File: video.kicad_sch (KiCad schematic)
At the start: 75 parts, among them IC11 MC14053, IC14 74LS86AN, IC21 74LS74, IC22 74LS00N, IC23 74ALS74N, IC27 74LS20N, IC28 74LS393N, IC29 74LS393N, IC30 74LS32N, IC32 74LS390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

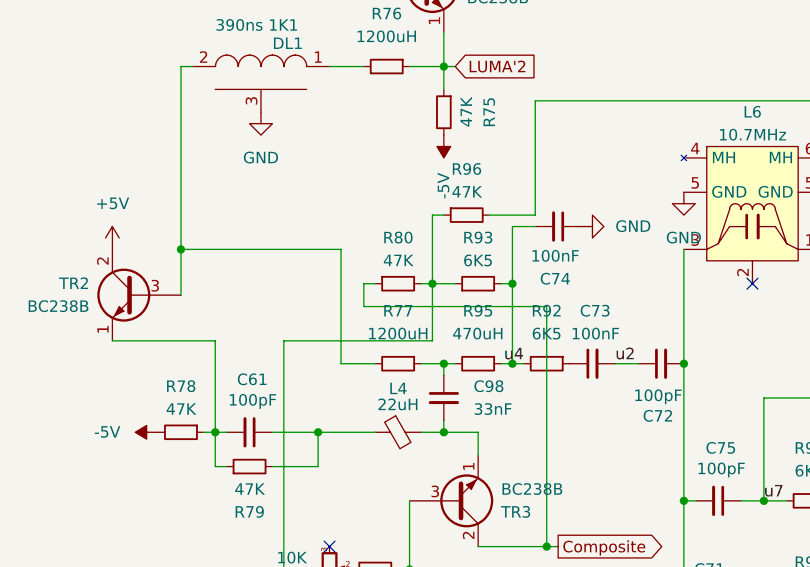
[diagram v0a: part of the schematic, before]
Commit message: add missing power connections
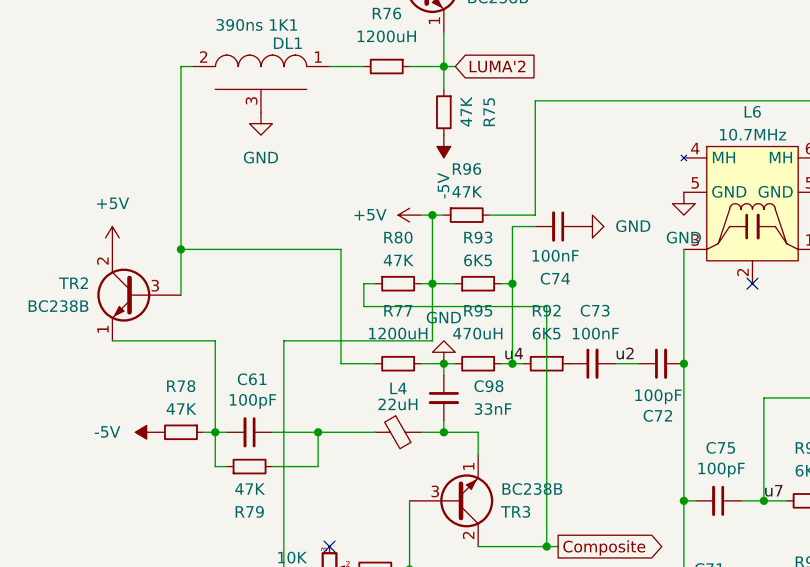
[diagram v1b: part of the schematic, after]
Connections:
- net +5V: now also R80.2, R82.1, R93.1, R96.1
- net GND: now also C98.1, R77.1, R95.2
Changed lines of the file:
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@@
 	)
 	(junction
+		(at 349.25 60.96)
+		(diameter 0)
+		(color 0 0 0 0)
+	)
+	(junction
 		(at 346.71 100.33)
 		(diameter 0)
@@
 	(wire
 		(pts
+			(xy 347.98 60.96) (xy 349.25 60.96)
+		)
+		(stroke
+			(width 0)
+			(type default)
+		)
+	)
+	(wire
+		(pts
 			(xy 143.51 89.535) (xy 145.669 89.535)
 		)
@@
 	)
 	(symbol
-		(lib_name "vdg:TOKO_Variable_Inductor")
 		(lib_id "vdg:TOKO_Variable_Inductor")
 		(at 384.81 58.42 0)
@@
 	)
 	(symbol
+		(lib_id "power:GND")
+		(at 350.52 77.47 0)
+		(mirror x)
+		(unit 1)
+		(exclude_from_sim no)
+		(in_bom yes)
+		(on_board yes)
+		(dnp no)
+		(fields_autoplaced yes)
+		(property "Reference" "#PWR0196"
+			(at 350.52 71.12 0)
+			(effects
+				(font
+					(size 1.27 1.27)
+				)
+				(hide yes)
+			)
+		)
+		(property "Value" "GND"
+			(at 350.52 72.39 0)
+			(effects
+				(font
+					(size 1.27 1.27)
+				)
+			)
+		)
+		(property "Footprint" ""
+			(at 350.52 77.47 0)
+			(effects
+				(font
+					(size 1.27 1.27)
+				)
+				(hide yes)
+			)
+		)
+		(property "Datasheet" ""
+			(at 350.52 77.47 0)
+			(effects
+				(font
+					(size 1.27 1.27)
+				)
+				(hide yes)
+			)
+		)
+		(property "Description" ""
+			(at 350.52 77.47 0)
+			(effects
+				(font
+					(size 1.27 1.27)
+				)
+				(hide yes)
+			)
+		)
+		(pin "1"
+		)
+		(instances
+			(project "Dragon32Issue2ASecam"
+				(path "/e3d9e4a2-26cb-4482-98c1-138d9a22d1eb/abc062f3-c6ab-4360-94b7-a88968b74324"
+					(reference "#PWR0196")
+					(unit 1)
+				)
+			)
+		)
+	)
+	(symbol
 		(lib_id "Device:R_Small")
 		(at 344.17 44.45 270)
@@
 	)
 	(symbol
-		(lib_name "vdg:TOKO_Variable_Inductor")
 		(lib_id "vdg:TOKO_Variable_Inductor")
 		(at 384.81 -16.51 0)
@@
 					(unit 1)
 				)
+			)
+		)
+	)
+	(symbol
+		(lib_id "power:+5V")
+		(at 347.98 60.96 90)
+		(unit 1)
+		(exclude_from_sim no)
+		(in_bom yes)
+		(on_board yes)
+		(dnp no)
+		(fields_autoplaced yes)
+		(property "Reference" "#PWR0197"
+			(at 351.79 60.96 0)
+			(effects
+				(font
+					(size 1.27 1.27)
+				)
+				(hide yes)
+			)
+		)
+		(property "Value" "+5V"
+			(at 344.17 60.9599 90)
+			(effects
+				(font
+					(size 1.27 1.27)
+				)
+				(justify left)
+			)
+		)
+		(property "Footprint" ""
+			(at 347.98 60.96 0)
+			(effects
+				(font
+					(size 1.27 1.27)
+				)
+				(hide yes)
+			)
+		)
+		(property "Datasheet" ""
+			(at 347.98 60.96 0)
+			(effects
+				(font
+					(size 1.27 1.27)
+				)
+				(hide yes)
+			)
+		)
+		(property "Description" ""
+			(at 347.98 60.96 0)
+			(effects
+				(font
+					(size 1.27 1.27)
+				)
+				(hide yes)
+			)
+		)
+		(pin "1"
+		)
+		(instances
+			(project "Dragon32Issue2ASecam"
+				(path "/e3d9e4a2-26cb-4482-98c1-138d9a22d1eb/abc062f3-c6ab-4360-94b7-a88968b74324"
+					(reference "#PWR0197")
+					(unit 1)
+				)
